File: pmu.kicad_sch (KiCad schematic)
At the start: 4 parts, among them SW1 Power ON SW, U2 MAX1555

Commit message: more stuff
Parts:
- added C16: 100n, Capacitor_SMD:C_0805_2012Metric, symbol Device:C
- added C17, C18: 10uF/10V, Capacitor_Tantalum_SMD:CP_EIA-3528-21_Kemet-B, symbol Device:C_Polarized
- added J5: Battery, symbol Connector:Conn_01x04_Pin
- added L1: 1u5, Inductor_SMD:L_1210_3225Metric, symbol Device:L
- added Q3: BSS138, Package_TO_SOT_SMD:SOT-23, symbol Transistor_FET:BSS138
- added Q4: BSS84, Package_TO_SOT_SMD:SOT-23, symbol Transistor_FET:BSS84
- added R22, R23, R24: 100k, Inductor_SMD:L_0805_2012Metric, symbol Device:R
- added U4: TPS63030DSK, Package_SON:WSON-10-1EP_2.5x2.5mm_P0.5mm_EP1.2x2mm, symbol Regulator_Switching:TPS63030DSK
- SW1: value Power ON SW -> ~
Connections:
- net 5V_USB: now also D9.2 (A)
- net GND: now also C16.1, C17.2, C18.2, J5.1 (Pin_1), Q4.3 (D), R22.1, R24.1, U4.11 (PGND), U4.3 (PGND), U4.9 (GND)
- net ~{CHG}: now reaches U2.3 (~{CHG})
- net at U2.5 (BAT): now also D10.2 (A), J5.4 (Pin_4)
- net at D9.1 (K): now also D10.1 (K), SW1.2, SW1.4 (A), Q3.3 (D), R23.2, U4.5 (VIN)
- net at SW1.1: now also SW1.3 (K), Q3.2 (S), R22.2, U4.6 (EN)
- new net: L1.2, U4.2 (L2)
- new net: L1.1, U4.4 (L1)
- new net: C16.2, U4.7 (PS/SYNC), U4.8 (VINA)
- new net: Q3.1 (G), Q4.2 (S), R23.1
- new net +3V3: C17.1, C18.1, U4.1 (VOUT), U4.10 (FB)
- new net PWR_ON: Q4.1 (G), R24.2
- no-connect marks 0 -> 2
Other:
- note added: "BAT+"
- note added: "BAT-"
- note added: "BSI"
- note added: "Power ON"
- note added: "TEMP"
- moved on the sheet: D10, D9, SW1, U2

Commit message: imported SA868 - thanks, edgetriggered
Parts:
- added BT1: Battery_Cell, symbol Device:Battery_Cell
- added D3: BAT60A, Diode_SMD:D_SOD-323, symbol Diode:BAT60A
- added R6: 1k, Inductor_SMD:L_0805_2012Metric, symbol Device:R
- renumbered C16 to C11, C17 to C12, C18 to C13, D9 to D1, D10 to D2, J5 to J3, Q4 to Q1, Q3 to Q2, R23 to R3, R24 to R4, R22 to R5, U2 to U3
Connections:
- net +3V3: now also D3.2 (A)
- net GND: now also BT1.2 (-)
- net U_BATT: now reaches D2.2 (A), J3.4 (Pin_4), U3.5 (BAT)
- new net: D3.1 (K), R6.2
- new net RTC_BATT: BT1.1 (+), R6.1
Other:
- moved on the sheet: C11, C12, C13, D1, D2, J3, L1, Q1, Q2, R3, R4, R5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

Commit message: connections
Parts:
- R9: renamed from R5; value 100k -> 47k
- SW1: value ~ -> POWER ON
- renumbered D1 to D2, D2 to D3, D3 to D4, J3 to J4, R6 to R10, R3 to R7, R4 to R8
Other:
- note removed: "Power ON"
- moved on the sheet: Q1, Q2, R8

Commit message: audio part
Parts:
- removed Q1: BSS84, Package_TO_SOT_SMD:SOT-23, symbol Transistor_FET:BSS84
- removed Q2: BSS138, Package_TO_SOT_SMD:SOT-23, symbol Transistor_FET:BSS138
- added Q3: BSS138, Package_TO_SOT_SMD:SOT-23, symbol Transistor_FET:BSS138
- added Q4: BSS84, Package_TO_SOT_SMD:SOT-23, symbol Transistor_FET:BSS84
- renumbered R8 to R10, R9 to R11, R10 to R12, R7 to R9
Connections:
- net GND: now also Q3.2 (S)
- net PWR_ON: now also Q3.1 (G)
- net at D2.1 (K), D3.1 (K), R9.2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: now also Q4.2 (S)
- net at R11.2, SW1.1, SW1.3 (K)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: now also Q4.3 (D)
- net at R9.1: now also Q3.3 (D), Q4.1 (G)

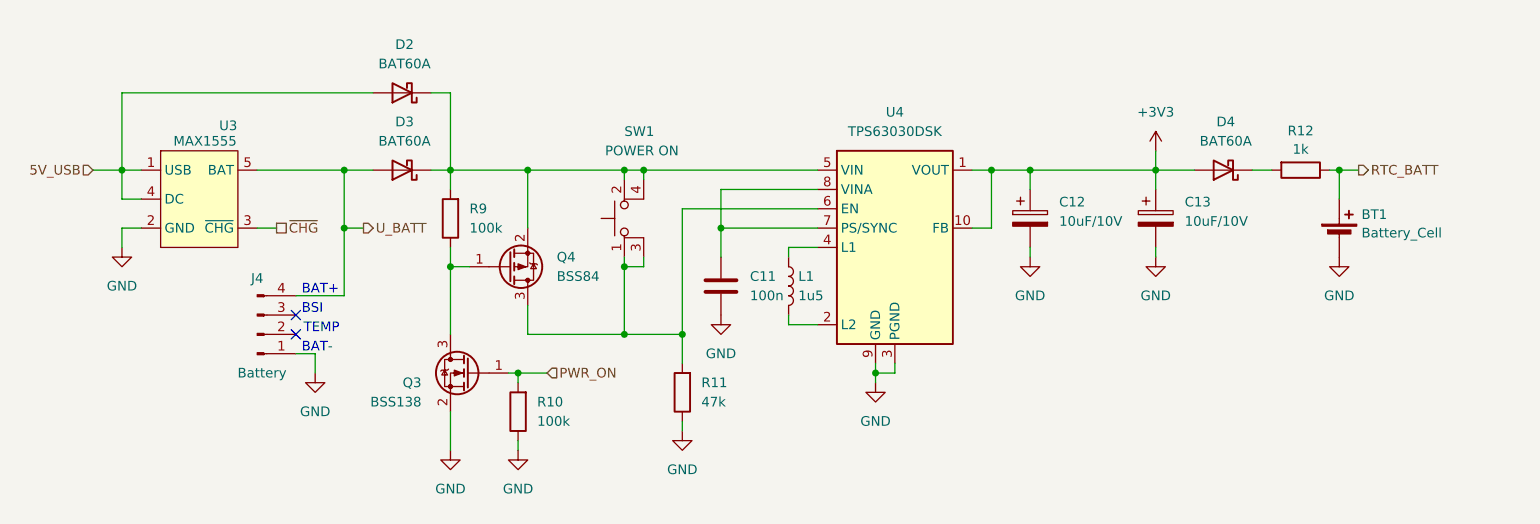
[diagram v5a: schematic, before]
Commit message: spk/mic update
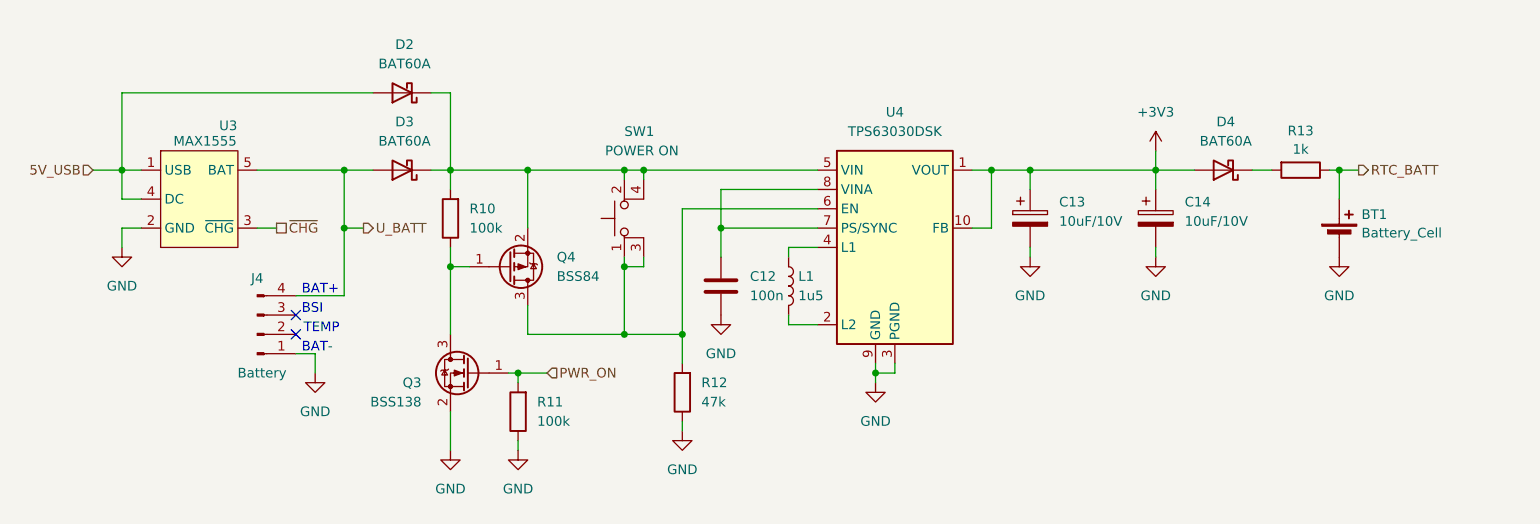
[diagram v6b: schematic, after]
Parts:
- renumbered C11 to C12, C12 to C13, C13 to C14, R9 to R10, R10 to R11, R11 to R12, R12 to R13
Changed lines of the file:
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@@
 	(title_block
 		(title "Mainboard replacement for Nokia 3310")
-		(date "25-10-2024")
+		(date "28-10-2024")
 		(rev "Rev A")
 		(company "M17 Project")
@@
 		(dnp no)
 		(fields_autoplaced yes)
-		(property "Reference" "#PWR036"
+		(property "Reference" "#PWR037"
 			(at 196.85 104.14 0)
 			(effects
@@
 			(project "M17_3310"
 				(path "/8d65c5ef-7a02-4454-aee5-ab9c49e4aeab/69b4d1b1-805b-4c7a-b583-ffe559937ec6"
-					(reference "#PWR036")
+					(reference "#PWR037")
 					(unit 1)
 				)
@@
 		(dnp no)
 		(fields_autoplaced yes)
-		(property "Reference" "R10"
+		(property "Reference" "R11"
 			(at 115.5304 116.8399 0)
 			(effects
@@
 			(project "M17_3310"
 				(path "/8d65c5ef-7a02-4454-aee5-ab9c49e4aeab/69b4d1b1-805b-4c7a-b583-ffe559937ec6"
-					(reference "R10")
+					(reference "R11")
 					(unit 1)
 				)
@@
 		(dnp no)
 		(fields_autoplaced yes)
-		(property "Reference" "#PWR037"
+		(property "Reference" "#PWR038"
 			(at 220.98 104.14 0)
 			(effects
@@
 			(project "M17_3310"
 				(path "/8d65c5ef-7a02-4454-aee5-ab9c49e4aeab/69b4d1b1-805b-4c7a-b583-ffe559937ec6"
-					(reference "#PWR037")
+					(reference "#PWR038")
 					(unit 1)
 				)
@@
 		(dnp no)
 		(fields_autoplaced yes)
-		(property "Reference" "R11"
+		(property "Reference" "R12"
 			(at 137.1204 114.2999 0)
 			(effects
@@
 			(project "M17_3310"
 				(path "/8d65c5ef-7a02-4454-aee5-ab9c49e4aeab/69b4d1b1-805b-4c7a-b583-ffe559937ec6"
-					(reference "R11")
+					(reference "R12")
 					(unit 1)
 				)
@@
 		(dnp no)
 		(fields_autoplaced yes)
-		(property "Reference" "#PWR029"
+		(property "Reference" "#PWR030"
 			(at 104.14 129.54 0)
 			(effects
@@
 			(project "M17_3310"
 				(path "/8d65c5ef-7a02-4454-aee5-ab9c49e4aeab/69b4d1b1-805b-4c7a-b583-ffe559937ec6"
-					(reference "#PWR029")
+					(reference "#PWR030")
 					(unit 1)
 				)
@@
 		(dnp no)
 		(fields_autoplaced yes)
-		(property "Reference" "C11"
+		(property "Reference" "C12"
 			(at 143.51 100.3299 0)
 			(effects
@@
 			(project "M17_3310"
 				(path "/8d65c5ef-7a02-4454-aee5-ab9c49e4aeab/69b4d1b1-805b-4c7a-b583-ffe559937ec6"
-					(reference "C11")
+					(reference "C12")
 					(unit 1)
 				)
@@
 		(dnp no)
 		(fields_autoplaced yes)
-		(property "Reference" "#PWR032"
+		(property "Reference" "#PWR033"
 			(at 139.7 111.76 0)
 			(effects
@@
 			(project "M17_3310"
 				(path "/8d65c5ef-7a02-4454-aee5-ab9c49e4aeab/69b4d1b1-805b-4c7a-b583-ffe559937ec6"
-					(reference "#PWR032")
+					(reference "#PWR033")
 					(unit 1)
 				)
@@
 		(dnp no)
 		(fields_autoplaced yes)
-		(property "Reference" "#PWR028"
+		(property "Reference" "#PWR029"
 			(at 86.36 119.38 0)
 			(effects
@@
 			(project "M17_3310"
 				(path "/8d65c5ef-7a02-4454-aee5-ab9c49e4aeab/69b4d1b1-805b-4c7a-b583-ffe559937ec6"
-					(reference "#PWR028")
+					(reference "#PWR029")
 					(unit 1)
 				)
@@
 		(dnp no)
 		(fields_autoplaced yes)
-		(property "Reference" "#PWR033"
+		(property "Reference" "#PWR034"
 			(at 160.02 120.65 0)
 			(effects
@@
 			(project "M17_3310"
 				(path "/8d65c5ef-7a02-4454-aee5-ab9c49e4aeab/69b4d1b1-805b-4c7a-b583-ffe559937ec6"
-					(reference "#PWR033")
+					(reference "#PWR034")
 					(unit 1)
 				)
@@
 		(dnp no)
 		(fields_autoplaced yes)
-		(property "Reference" "R9"
+		(property "Reference" "R10"
 			(at 106.6404 91.4399 0)
 			(effects
@@
 			(project "M17_3310"
 				(path "/8d65c5ef-7a02-4454-aee5-ab9c49e4aeab/69b4d1b1-805b-4c7a-b583-ffe559937ec6"
-					(reference "R9")
+					(reference "R10")
 					(unit 1)
 				)
@@
 		(dnp no)
 		(fields_autoplaced yes)
-		(property "Reference" "C13"
+		(property "Reference" "C14"
 			(at 200.66 90.5509 0)
 			(effects
@@
 			(project "M17_3310"
 				(path "/8d65c5ef-7a02-4454-aee5-ab9c49e4aeab/69b4d1b1-805b-4c7a-b583-ffe559937ec6"
-					(reference "C13")
+					(reference "C14")
 					(unit 1)
 				)
@@
 		(dnp no)
 		(fields_autoplaced yes)
-		(property "Reference" "#PWR031"
+		(property "Reference" "#PWR032"
 			(at 134.62 127 0)
 			(effects
@@
 			(project "M17_3310"
 				(path "/8d65c5ef-7a02-4454-aee5-ab9c49e4aeab/69b4d1b1-805b-4c7a-b583-ffe559937ec6"
-					(reference "#PWR031")
+					(reference "#PWR032")
 					(unit 1)
 				)
@@
 		(dnp no)
 		(fields_autoplaced yes)
-		(property "Reference" "#PWR034"
+		(property "Reference" "#PWR035"
 			(at 180.34 104.14 0)
 			(effects
@@
 			(project "M17_3310"
 				(path "/8d65c5ef-7a02-4454-aee5-ab9c49e4aeab/69b4d1b1-805b-4c7a-b583-ffe559937ec6"
-					(reference "#PWR034")
+					(reference "#PWR035")
 					(unit 1)
 				)
@@
 		(dnp no)
 		(fields_autoplaced yes)
-		(property "Reference" "C12"
+		(property "Reference" "C13"
 			(at 184.15 90.5509 0)
 			(effects
@@
 			(project "M17_3310"
 				(path "/8d65c5ef-7a02-4454-aee5-ab9c49e4aeab/69b4d1b1-805b-4c7a-b583-ffe559937ec6"
-					(reference "C12")
+					(reference "C13")
 					(unit 1)
 				)
@@
 		(dnp no)
 		(fields_autoplaced yes)
-		(property "Reference" "#PWR035"
+		(property "Reference" "#PWR036"
 			(at 196.85 87.63 0)
 			(effects
@@
 			(project ""
 				(path "/8d65c5ef-7a02-4454-aee5-ab9c49e4aeab/69b4d1b1-805b-4c7a-b583-ffe559937ec6"
-					(reference "#PWR035")
+					(reference "#PWR036")
 					(unit 1)
 				)
@@
 		(dnp no)
 		(fields_autoplaced yes)
-		(property "Reference" "R12"
+		(property "Reference" "R13"
 			(at 215.9 81.1995 90)
 			(effects
@@
 			(project "M17_3310"
 				(path "/8d65c5ef-7a02-4454-aee5-ab9c49e4aeab/69b4d1b1-805b-4c7a-b583-ffe559937ec6"
-					(reference "R12")
+					(reference "R13")
 					(unit 1)
 				)
@@
 		(dnp no)
 		(fields_autoplaced yes)
-		(property "Reference" "#PWR027"
+		(property "Reference" "#PWR028"
 			(at 60.96 102.87 0)
 			(effects
@@
 			(project ""
 				(path "/8d65c5ef-7a02-4454-aee5-ab9c49e4aeab/69b4d1b1-805b-4c7a-b583-ffe559937ec6"
-					(reference "#PWR027")
+					(reference "#PWR028")
 					(unit 1)
 				)
@@
 		(dnp no)
 		(fields_autoplaced yes)
-		(property "Reference" "#PWR030"
+		(property "Reference" "#PWR031"
 			(at 113.03 129.54 0)
 			(effects
@@
 			(project "M17_3310"
 				(path "/8d65c5ef-7a02-4454-aee5-ab9c49e4aeab/69b4d1b1-805b-4c7a-b583-ffe559937ec6"
-					(reference "#PWR030")
+					(reference "#PWR031")
 					(unit 1)
 				)

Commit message: removed audio part
- added buzzer
- added battery voltage measurement
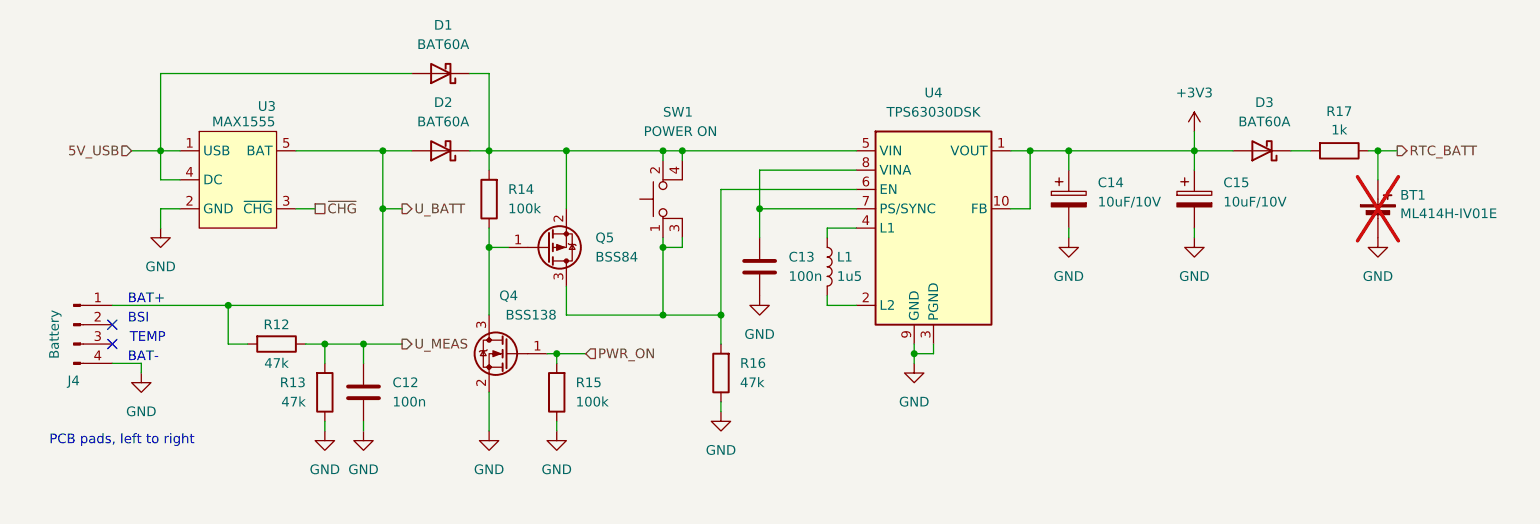
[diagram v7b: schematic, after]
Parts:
- added C12: 100n, Capacitor_SMD:C_0805_2012Metric, symbol Device:C
- added R12, R13: 47k, Inductor_SMD:L_0805_2012Metric, symbol Device:R
- BT1: value Battery_Cell -> ML414H-IV01E; now not fitted; now left out of the parts list
- renumbered C12 to C13, C13 to C14, C14 to C15, D2 to D1, D3 to D2, D4 to D3, Q3 to Q4, Q4 to Q5, R10 to R14, R11 to R15, R12 to R16, R13 to R17
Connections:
- net GND: now also J4.4 (Pin_4), C12.1, R13.1; no longer J4.1 (Pin_1)
- net U_BATT: now also J4.1 (Pin_1), R12.2; no longer J4.4 (Pin_4)
- new net U_MEAS: C12.2, R12.1, R13.2
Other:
- note added: "PCB pads, left to right"
- moved on the sheet: C13, C14, C15, D1, D2, D3, J4, L1, Q4, Q5, R14, R15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
